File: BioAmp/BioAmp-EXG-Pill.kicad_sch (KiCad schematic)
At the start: 41 parts, among them IC3 MAX1169BEUD+, J1 Conn_01x03_Pin, J2 Conn_01x04_Pin, J3 Conn_01x04_Pin, U1 Amp, U10 TPD1E05U06DPY, U11 TPD1E05U06DPY, U12 TPD1E05U06DPY, U3 TPD1E05U06DPY, U4 TPD1E05U06DPY, U6 TPD1E05U06DPY

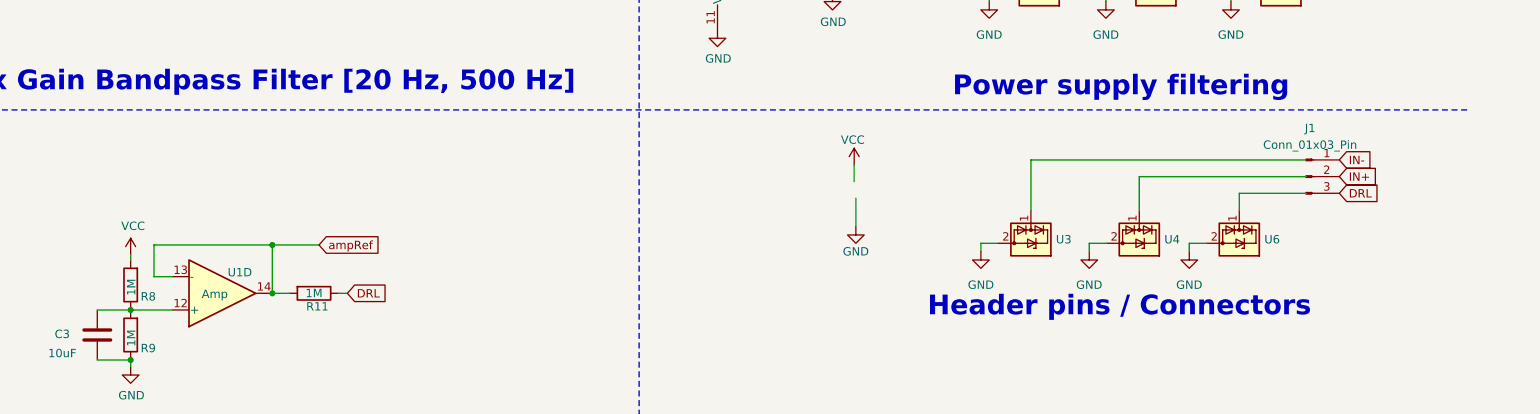
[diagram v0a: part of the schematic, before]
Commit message: Fixed ESD protection on J1 (connections were on the wrong side).
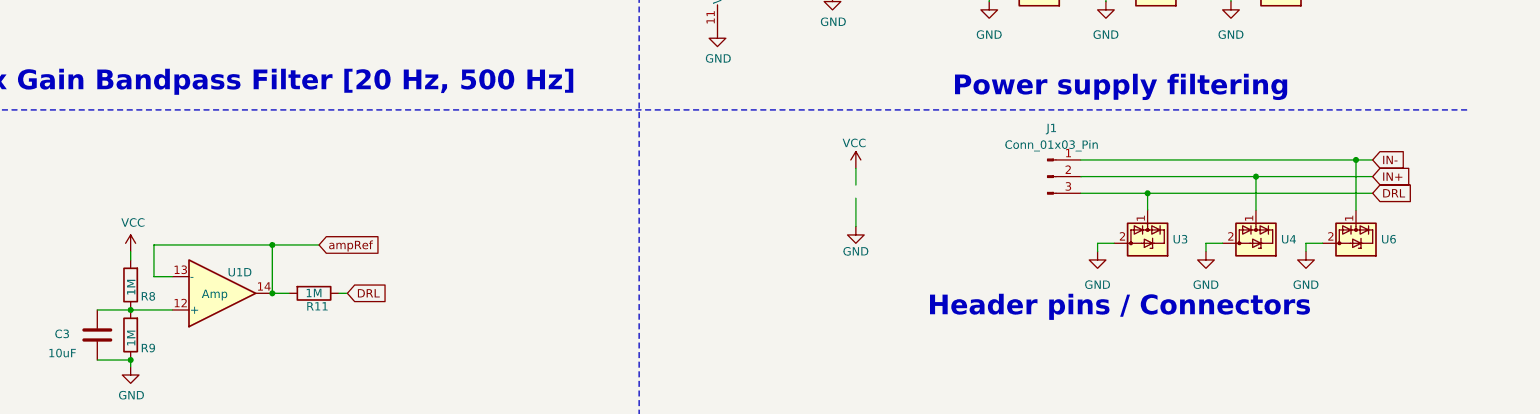
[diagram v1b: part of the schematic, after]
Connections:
- net DRL: now also U3.1 (I/O)
- net IN+: now also U4.1 (I/O)
- net IN-: now also U6.1 (I/O)
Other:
- moved on the sheet: J1, U3, U4, U6

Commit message: Added series resitors on all electrode connection pins for current limiting
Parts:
- removed R12: 2.2K, Resistor_SMD:R_0603_1608Metric_Pad0.98x0.95mm_HandSolder, symbol Device:R
- removed U3: TPD1E05U06DPY, Package_SON:Texas_DPY0002A_0.6x1mm_P0.65mm, symbol Power_Protection:TPD1E05U06DPY
- added R13, R14, R15, R20: 470k, Resistor_SMD:R_0603_1608Metric_Pad0.98x0.95mm_HandSolder, symbol Device:R
- added U5: TPD1E05U06DPY, Package_SON:Texas_DPY0002A_0.6x1mm_P0.65mm, symbol Power_Protection:TPD1E05U06DPY
- R11: value 1M -> 470k
- R6: value 2.2K -> 470k
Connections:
- net DRL: now also R20.1; no longer R11.1
- net GND: now also U5.2 (GND)
- net IN+: now also R15.2; no longer U4.1 (I/O)
- net IN-: no longer U6.1 (I/O)
- net ampRef: now also U5.1 (I/O)
- net at U1.5 (+): now also U4.1 (I/O), R14.1
- net at U1.3 (+): now also U6.1 (I/O), R13.1; no longer R6.1
- new net: R14.2, R15.1
- new net: R11.1, R20.2
- new net: R13.2, R6.1
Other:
- moved on the sheet: J1, R10, R6, R7, U1B

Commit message: Changed electrode resistances to one 1M
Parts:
- removed R15, R20, R6: 470k, Resistor_SMD:R_0603_1608Metric_Pad0.98x0.95mm_HandSolder, symbol Device:R
- R11, R13, R14: value 470k -> 1M
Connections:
- net DRL: now also R11.1
- net IN+: now also R14.2
- net IN-: now also R13.2
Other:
- moved on the sheet: R10, R14, U1B, U4

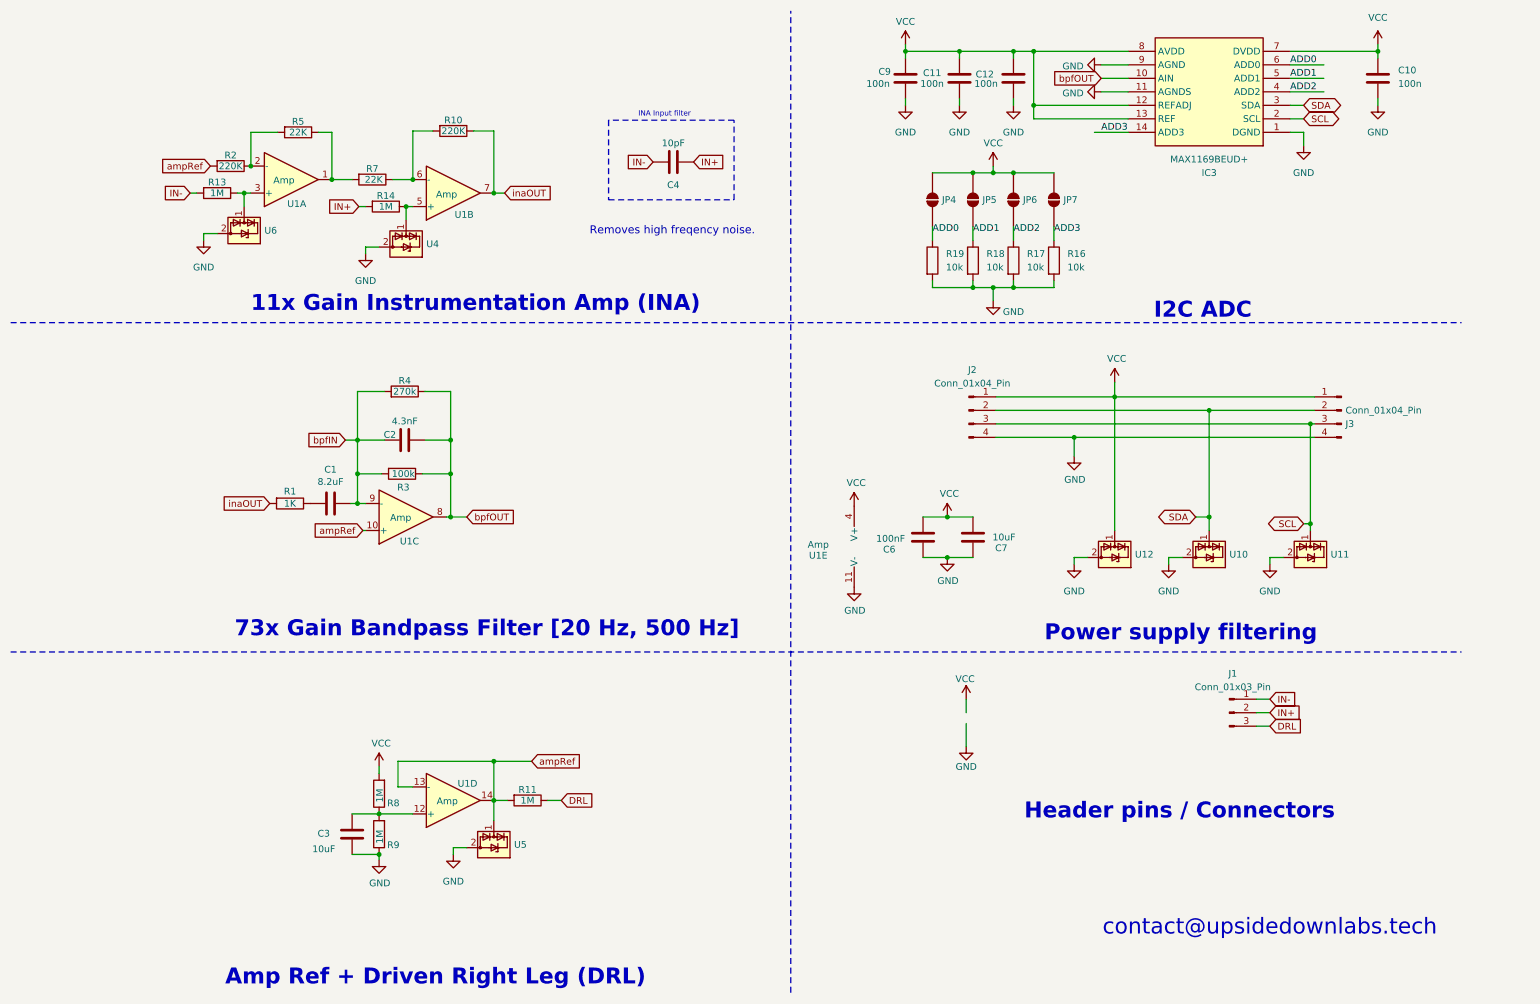
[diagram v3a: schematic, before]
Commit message: Changed TVS diodes to have lower clamping voltage and added series resitors after protected nodes on opamp
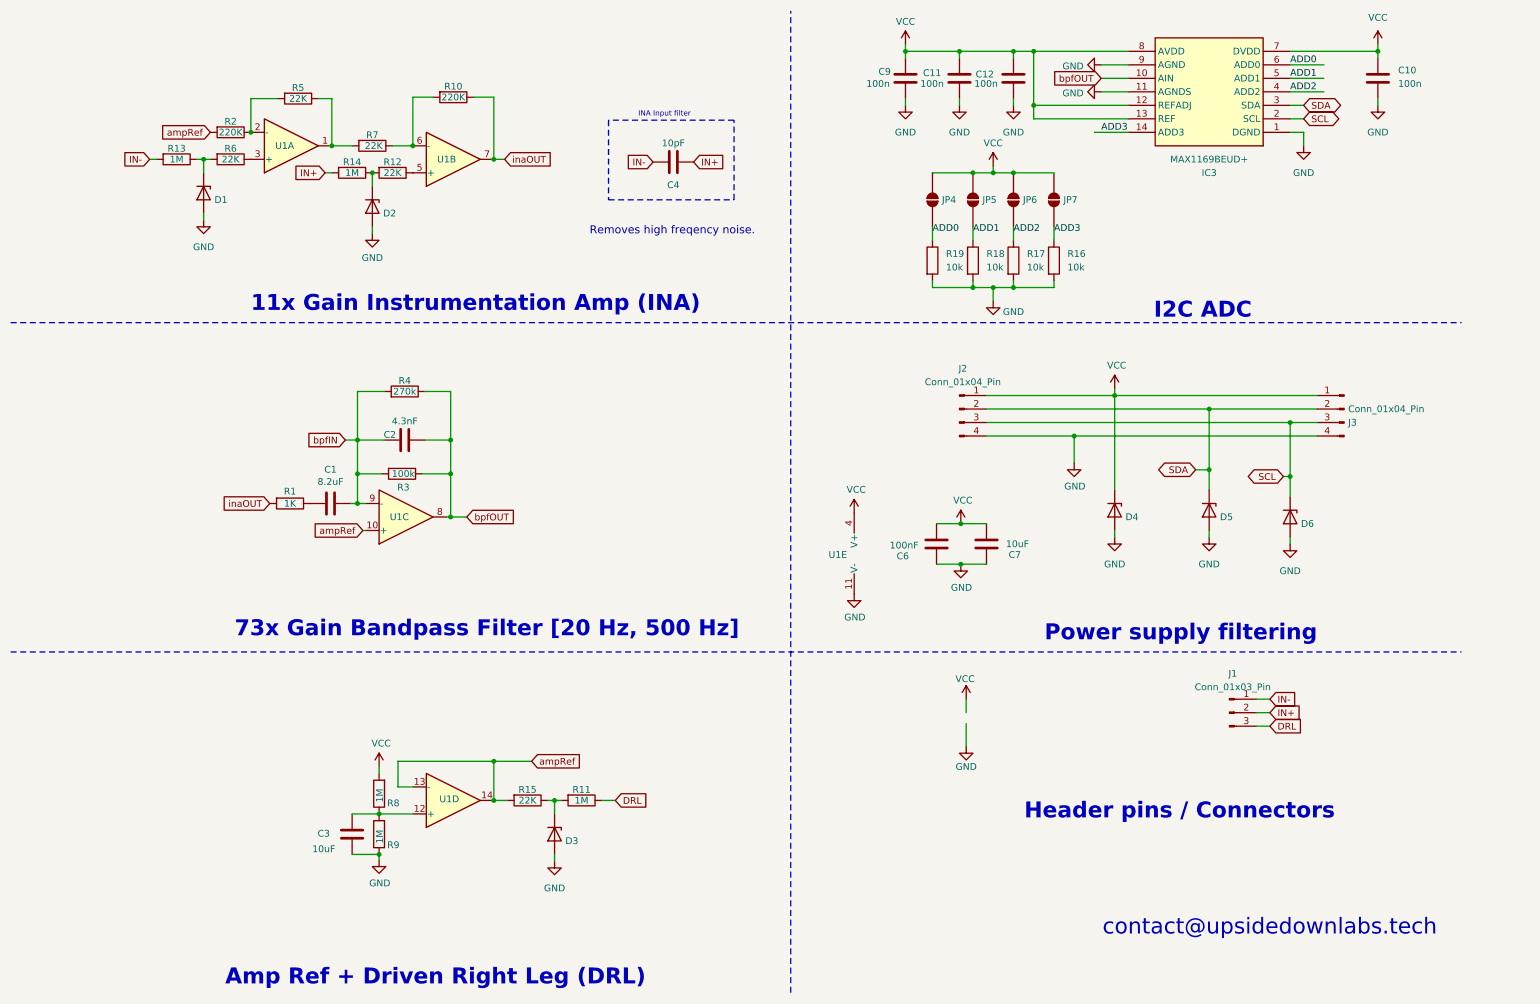
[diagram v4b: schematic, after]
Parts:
- removed U10, U11, U12, U4, U5, U6: TPD1E05U06DPY, Package_SON:Texas_DPY0002A_0.6x1mm_P0.65mm, symbol Power_Protection:TPD1E05U06DPY
- added D1, D2, D3, D4, D5, D6: ESD441DPYR, symbol Device:D_Zener
- added R12, R15, R6: 22K, Resistor_SMD:R_0603_1608Metric_Pad0.98x0.95mm_HandSolder, symbol Device:R
- U1: value Amp -> TL074HIPWR
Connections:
- net GND: now also D1.2 (A), D2.2 (A), D3.2 (A), D4.2 (A), D5.2 (A), D6.2 (A)
- net SCL: now also D6.1 (K)
- net SDA: now also D5.1 (K)
- net VCC: now also D4.1 (K)
- net ampRef: now also R15.2; no longer R11.2
- net at U1.5 (+): now also R12.1; no longer R14.1
- net at U1.3 (+): now also R6.1; no longer R13.1
- new net: D2.1 (K), R12.2, R14.1
- new net: D1.1 (K), R13.1, R6.2
- new net: D3.1 (K), R11.2, R15.1
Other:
- moved on the sheet: C6, C7, R10, R11, R13, R14, R2, R5, R7, U1A, U1B, U1E

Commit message: Changed IN+/IN- resistors to 500k to reduce noise. Refactored wiring that was off grid
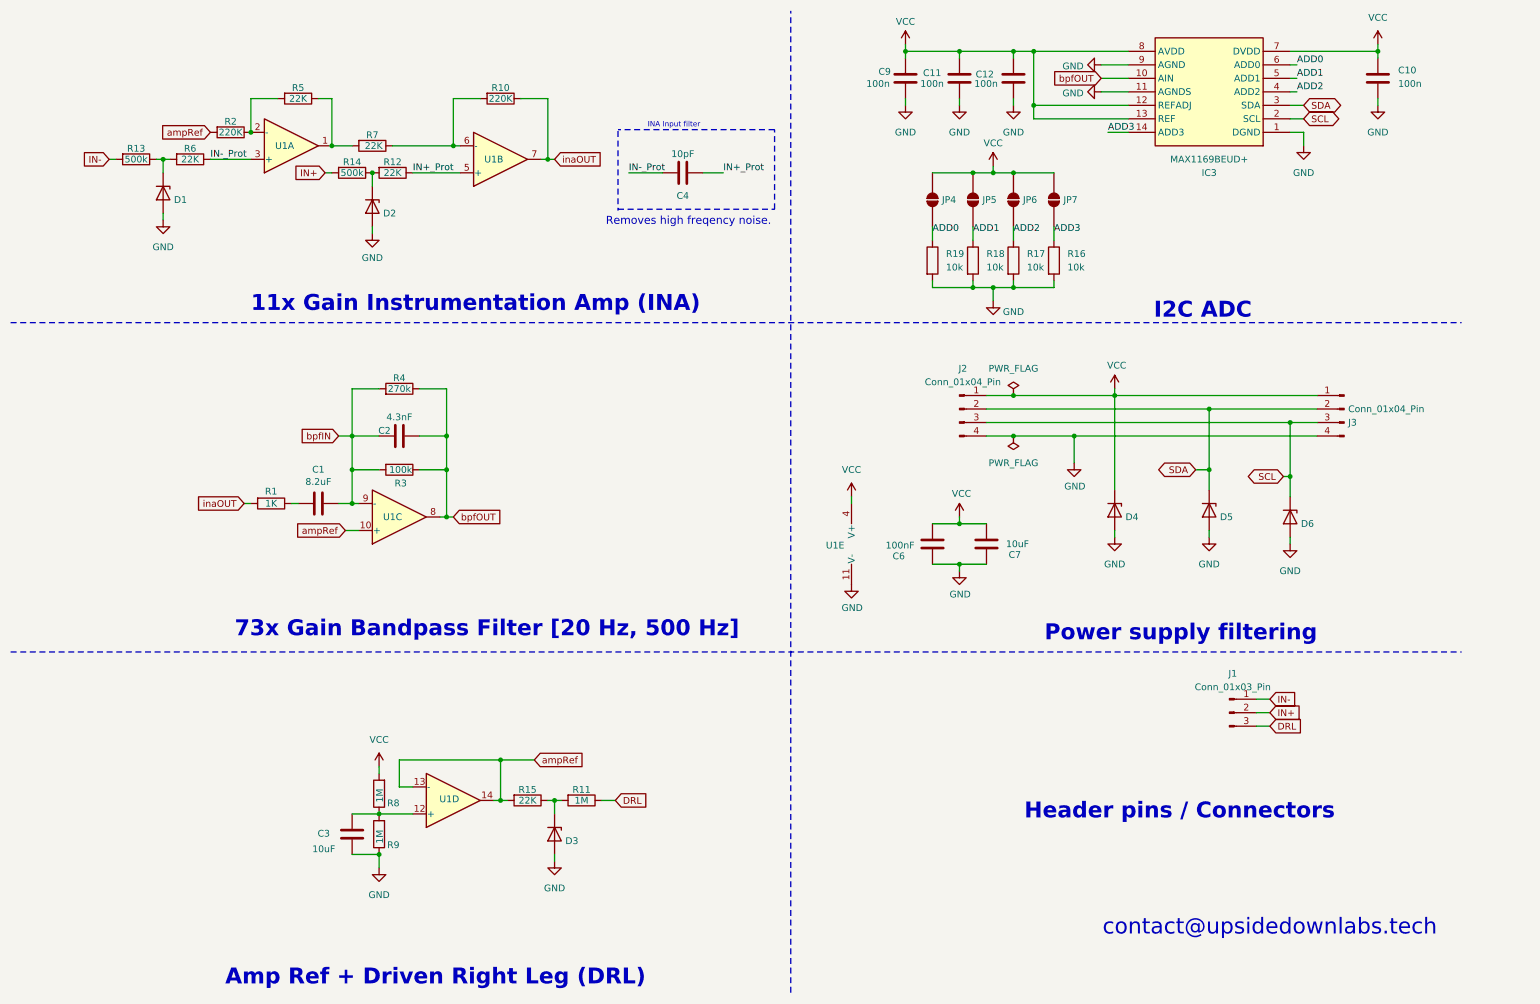
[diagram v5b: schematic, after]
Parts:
- R13, R14: value 1M -> 500k
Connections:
- net IN+: no longer C4.1
- net IN-: no longer C4.2
- net IN+_Prot: now reaches R12.1, U1.5 (+)
- net IN+_Prot: now also C4.1
- net IN-_Prot: now reaches R6.1, U1.3 (+)
- net IN-_Prot: now also C4.2
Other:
- moved on the sheet: C1, C2, C4, C6, D1, R1, R10, R13, R3, R4, R6, U1B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

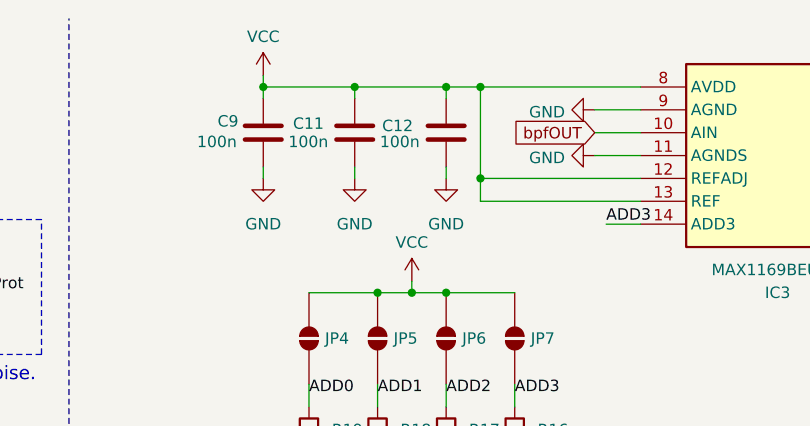
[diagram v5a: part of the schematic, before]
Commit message: Changed C12 to 10uF as per ADC datasheet recommendation
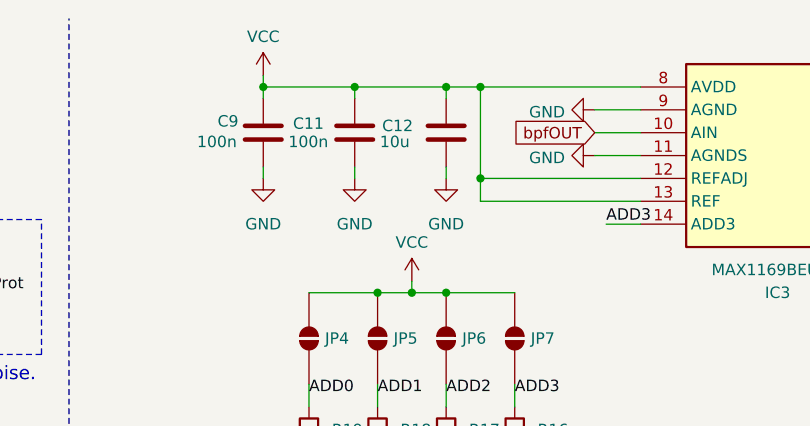
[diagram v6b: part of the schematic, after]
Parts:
- C12: value 100n -> 10u
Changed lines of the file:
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@@
 			)
 		)
-		(property "Value" "100n"
+		(property "Value" "10u"
 			(at 193.294 26.416 0)
 			(show_name no)

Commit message: Added ESD diode footprints
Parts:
- D1, D2, D3, D4, D5, D6: value ESD441DPYR -> ESD441DPLR; footprint (none) -> Diode_SMD:D_0201_0603Metric
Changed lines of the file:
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@@
 			)
 		)
-		(property "Value" "ESD441DPYR"
+		(property "Value" "ESD441DPLR"
 			(at 240.03 107.9499 90)
 			(hide yes)
@@
 			)
 		)
-		(property "Footprint" ""
+		(property "Footprint" "Diode_SMD:D_0201_0603Metric"
 			(at 237.49 106.68 0)
 			(hide yes)
@@
 			)
 		)
-		(property "Datasheet" "https://www.ti.com/lit/ds/symlink/esd441.pdf?ts=1790767769459&ref_url=https%253A%252F%252Fwww.mouser.ch%252F"
+		(property "Datasheet" "https://www.ti.com/lit/ds/symlink/esd441.pdf"
 			(at 237.49 106.68 0)
 			(hide yes)
@@
 			)
 		)
-		(property "Value" "ESD441DPYR"
+		(property "Value" "ESD441DPLR"
 			(at 222.25 107.9499 90)
 			(hide yes)
@@
 			)
 		)
-		(property "Footprint" ""
+		(property "Footprint" "Diode_SMD:D_0201_0603Metric"
 			(at 219.71 106.68 0)
 			(hide yes)
@@
 			)
 		)
-		(property "Value" "ESD441DPYR"
+		(property "Value" "ESD441DPLR"
 			(at 255.27 109.2199 90)
 			(hide yes)
@@
 			)
 		)
-		(property "Footprint" ""
+		(property "Footprint" "Diode_SMD:D_0201_0603Metric"
 			(at 252.73 107.95 0)
 			(hide yes)
@@
 			)
 		)
-		(property "Datasheet" "https://www.ti.com/lit/ds/symlink/esd441.pdf?ts=1790767769459&ref_url=https%253A%252F%252Fwww.mouser.ch%252F"
+		(property "Datasheet" "https://www.ti.com/lit/ds/symlink/esd441.pdf"
 			(at 252.73 107.95 0)
 			(hide yes)
@@
 			)
 		)
-		(property "Value" "ESD441DPYR"
+		(property "Value" "ESD441DPLR"
 			(at 116.84 168.9099 90)
 			(hide yes)
@@
 			)
 		)
-		(property "Footprint" ""
+		(property "Footprint" "Diode_SMD:D_0201_0603Metric"
 			(at 114.3 167.64 0)
 			(hide yes)
@@
 			)
 		)
-		(property "Datasheet" "https://www.ti.com/lit/ds/symlink/esd441.pdf?ts=1790767769459&ref_url=https%253A%252F%252Fwww.mouser.ch%252F"
+		(property "Datasheet" "https://www.ti.com/lit/ds/symlink/esd441.pdf"
 			(at 114.3 167.64 0)
 			(hide yes)
@@
 			)
 		)
-		(property "Value" "ESD441DPYR"
+		(property "Value" "ESD441DPLR"
 			(at 82.55 50.7999 90)
 			(hide yes)
@@
 			)
 		)
-		(property "Footprint" ""
+		(property "Footprint" "Diode_SMD:D_0201_0603Metric"
 			(at 80.01 49.53 0)
 			(hide yes)
@@
 			)
 		)
-		(property "Datasheet" "https://www.ti.com/lit/ds/symlink/esd441.pdf?ts=1790767769459&ref_url=https%253A%252F%252Fwww.mouser.ch%252F"
+		(property "Datasheet" "https://www.ti.com/lit/ds/symlink/esd441.pdf"
 			(at 80.01 49.53 0)
 			(hide yes)
@@
 			)
 		)
-		(property "Value" "ESD441DPYR"
+		(property "Value" "ESD441DPLR"
 			(at 43.18 48.2599 90)
 			(hide yes)
@@
 			)
 		)
-		(property "Footprint" ""
+		(property "Footprint" "Diode_SMD:D_0201_0603Metric"
 			(at 40.64 46.99 0)
 			(hide yes)
@@
 			)
 		)
-		(property "Datasheet" "https://www.ti.com/lit/ds/symlink/esd441.pdf?ts=1790767769459&ref_url=https%253A%252F%252Fwww.mouser.ch%252F"
+		(property "Datasheet" "https://www.ti.com/lit/ds/symlink/esd441.pdf"
 			(at 40.64 46.99 0)
 			(hide yes)
